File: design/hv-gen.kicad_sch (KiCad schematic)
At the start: 11 parts, among them Q1 Q_NMOS_DGS, T2 DA2033-AL, U5 TLP152TPL_E

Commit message: _
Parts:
- added R9: 50k, 1000V, symbol Device:R
- added U6: Optocoupler_DC, symbol Isolator:Optocoupler_DC_PhotoNPN_AKEC
- R5: value 600k -> 500k, 1000V
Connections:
- net Armed: now also U6.1
- net GND: now also U6.2
- net GNDHV: now also U6.3
- net HV+: now also R9.1
- new net: R9.2, U6.4

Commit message: _
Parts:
- removed U6: Optocoupler_DC, symbol Isolator:Optocoupler_DC_PhotoNPN_AKEC
- added Q2: Q_NMOS_DGS, symbol Transistor_FET:Q_NMOS_DGS
- added U6: TLP152TPL_E, TLP152_4P55X3P7_TOS, symbol project_symbols:TLP152TPL_E
- R5: value 500k, 1000V -> 1.5M, 1000V
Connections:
- net +22V: now also U6.6
- net Armed: now also U6.1
- net GND: now also U6.3
- net GNDFLY: now also U6.4
- net GNDHV: now also Q2.3 (S)
- net at R9.2: now also Q2.1 (D)
- new net: Q2.2 (G), U6.5
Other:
- note added: "TBH I'm not sure if I really need a fast discharge circuit. Maybe just an analog circuit to drive a warning LED in case the bank voltage is greater than like 10V"
- note removed: "To disable fast discharge circuit"
- moved on the sheet: R9

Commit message: _
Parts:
- removed Q2: Q_NMOS_DGS, symbol Transistor_FET:Q_NMOS_DGS
- removed R9: 50k, 1000V, symbol Device:R
- removed U6: TLP152TPL_E, TLP152_4P55X3P7_TOS, symbol project_symbols:TLP152TPL_E
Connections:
- net HVSense renamed HVVS
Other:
- note added: "HVCS should must be in range [0, COMP2_IN-]"
- note removed: "HVCS should must be in range [0, 1.2V]"
- note removed: "Maybe add a filter cap here"
- note removed: "TBH I'm not sure if I really need a fast discharge circuit. Maybe just an analog circuit to drive a warning LED in case the bank voltage is greater than like 10V"

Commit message: _
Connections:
- net +22V renamed +22V_Trans
- net +22V_Trans: no longer U5.6
- new net +22V_Drive: U5.6
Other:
- note added: "HVVS = HV+ * (R2/R2+R3) ~= HV+ * 0.001"
- note removed: "I need some way of providing strong isolation here"

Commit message: Working on high voltage switching
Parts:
- added D2: D, symbol Device:D
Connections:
- net +22V_Trans: now also D2.2 (A); no longer T2.10, T2.7, T2.8, T2.9
- new net: D2.1 (K), T2.10, T2.7, T2.8, T2.9
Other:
- company: UNH Resilient Architecture Lab -> University of New Hampshire, Resilient Architecture Lab
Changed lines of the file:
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@@
 		(title "BitCrusher: Affordable, Open Source EMFI Platform")
 		(rev "0.1")
-		(company "UNH Resilient Architecture Lab")
+		(company "University of New Hampshire, Resilient Architecture Lab")
 		(comment 1 "Advisor: Dean Sullivan")
 		(comment 2 "Author: George Crane")

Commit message: Continuing work on HV switching and primary power distribution
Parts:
- added C19, C21: 0.1u, symbol Device:C
- added C20: 4.7u, symbol Device:C
- added D6: D, symbol Device:D
- added Q3: PNP, symbol Simulation_SPICE:PNP
- added R9: R, symbol Device:R
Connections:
- net +22V_Drive: now also C19.1
- net GNDFLY: now also C19.2, C20.2, C21.2, Q3.1 (C)
- net at Q1.2 (G): now also D6.1 (K), Q3.3 (E); no longer U5.5
- new net: C20.1, C21.1
- new net: D6.2 (A), Q3.2 (B), R9.2
- new net: R9.1, U5.5
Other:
- note removed: "The flyback voltage will be present across the +22V line. A secondary voltage supply line for the flyback converter primary side would fix this"
- moved on the sheet: CBank1, C_CSF1, D1, D2, Q1, R2, R3, R5, RCS1, R_CSF1, T2, U5

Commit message: _
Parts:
- added CBank2, CBank3, CBank4, CBank5: 1u, symbol Device:C
- CBank1: value 5u -> 1u
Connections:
- net GNDHV: now also CBank2.2, CBank3.2, CBank4.2, CBank5.2
- net HV+: now also CBank2.1, CBank3.1, CBank4.1, CBank5.1
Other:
- note removed: "Review the TI gate driver app note and see if any turn-off circuit would be useful"
- moved on the sheet: R5

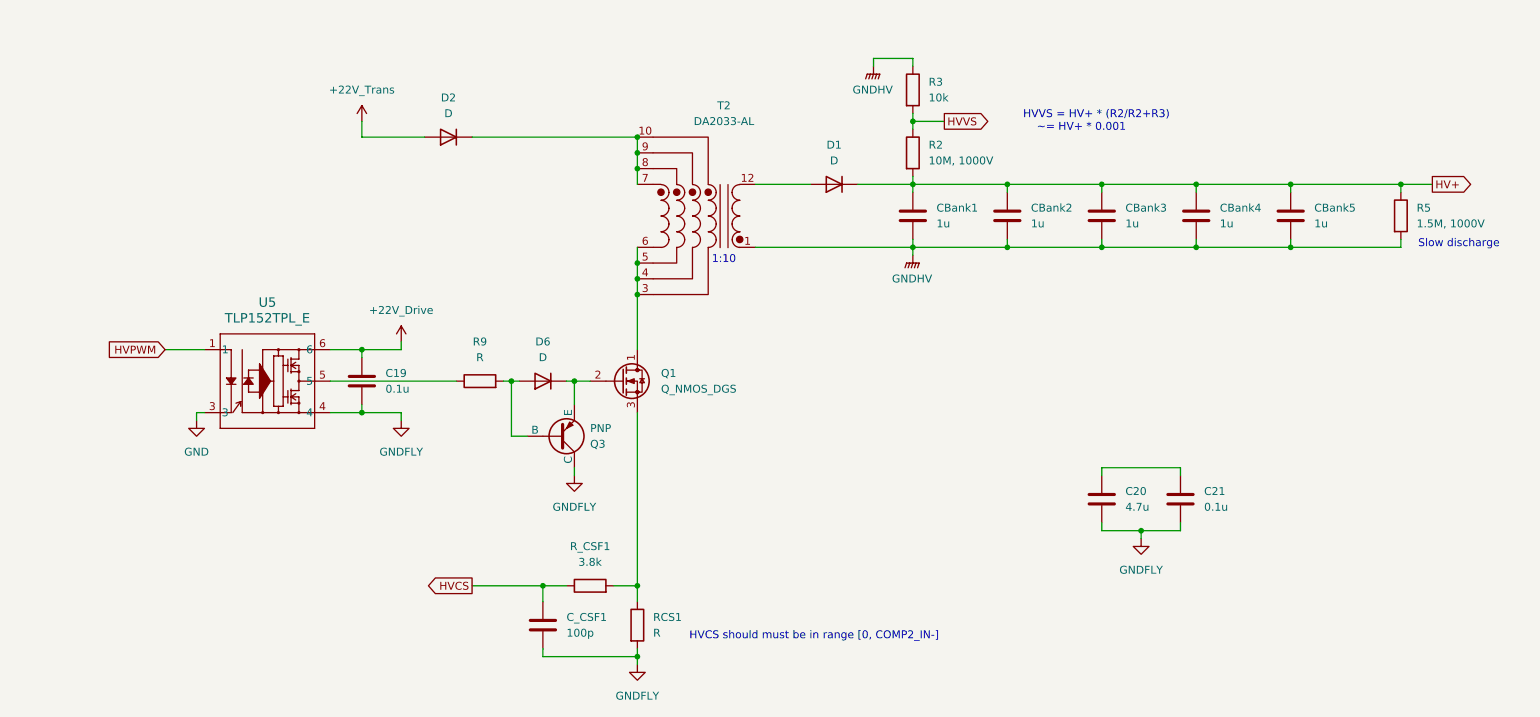
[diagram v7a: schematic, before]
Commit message: Finished flyback voltage sense divider
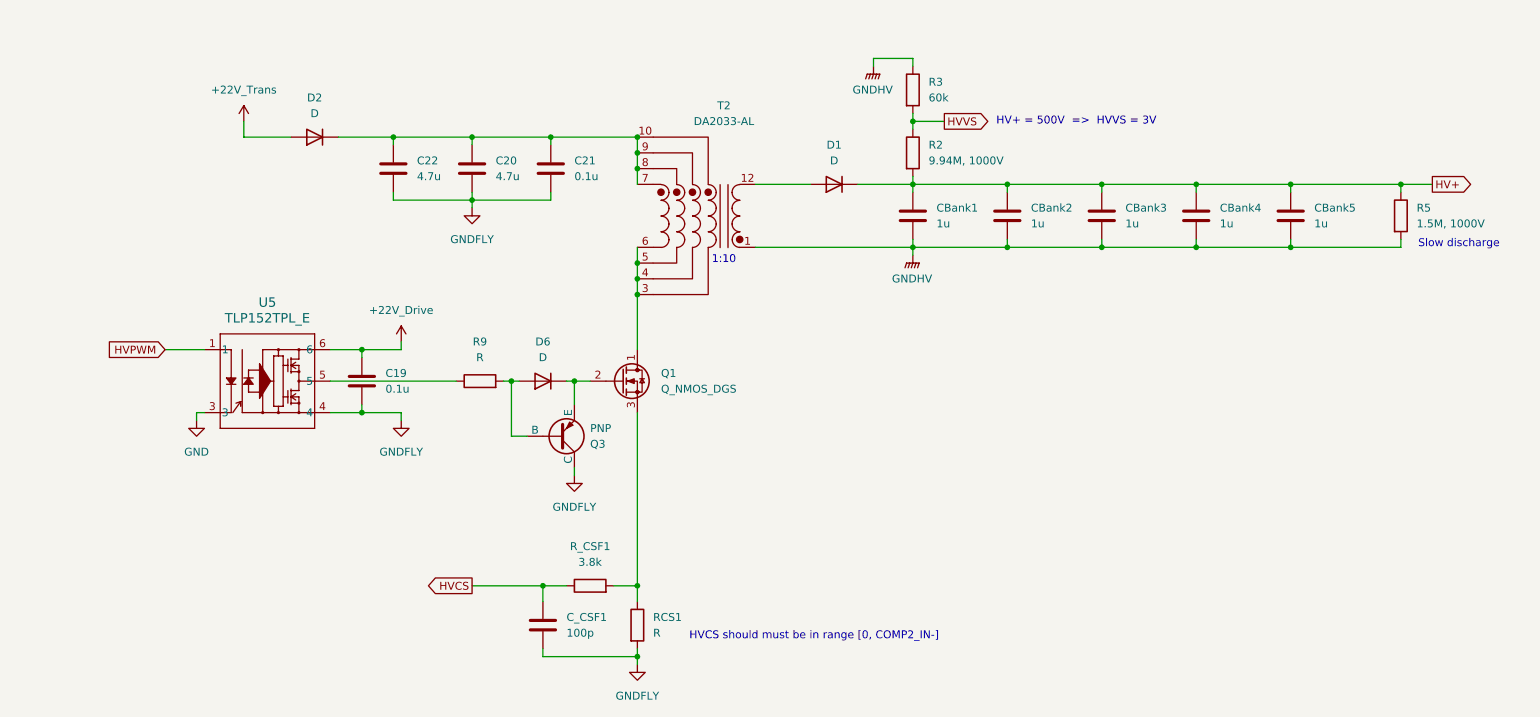
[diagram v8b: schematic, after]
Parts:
- added C22: 4.7u, symbol Device:C
- R2: value 10M, 1000V -> 9.94M, 1000V
- R3: value 10k -> 60k
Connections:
- net GNDFLY: now also C22.2
- net at C20.1, C21.1: now also D2.1 (K), T2.10, T2.7, T2.8, T2.9, C22.1
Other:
- note added: "HV+ = 500V => HVVS = 3V"
- note removed: "HVVS = HV+ * (R2/R2+R3) ~= HV+ * 0.001"
- moved on the sheet: C20, C21, D2
